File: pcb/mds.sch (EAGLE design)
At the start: 60 parts, among them IC1 MAX1555, U2 ISD1900ISD1932, U5 ATMEGA328

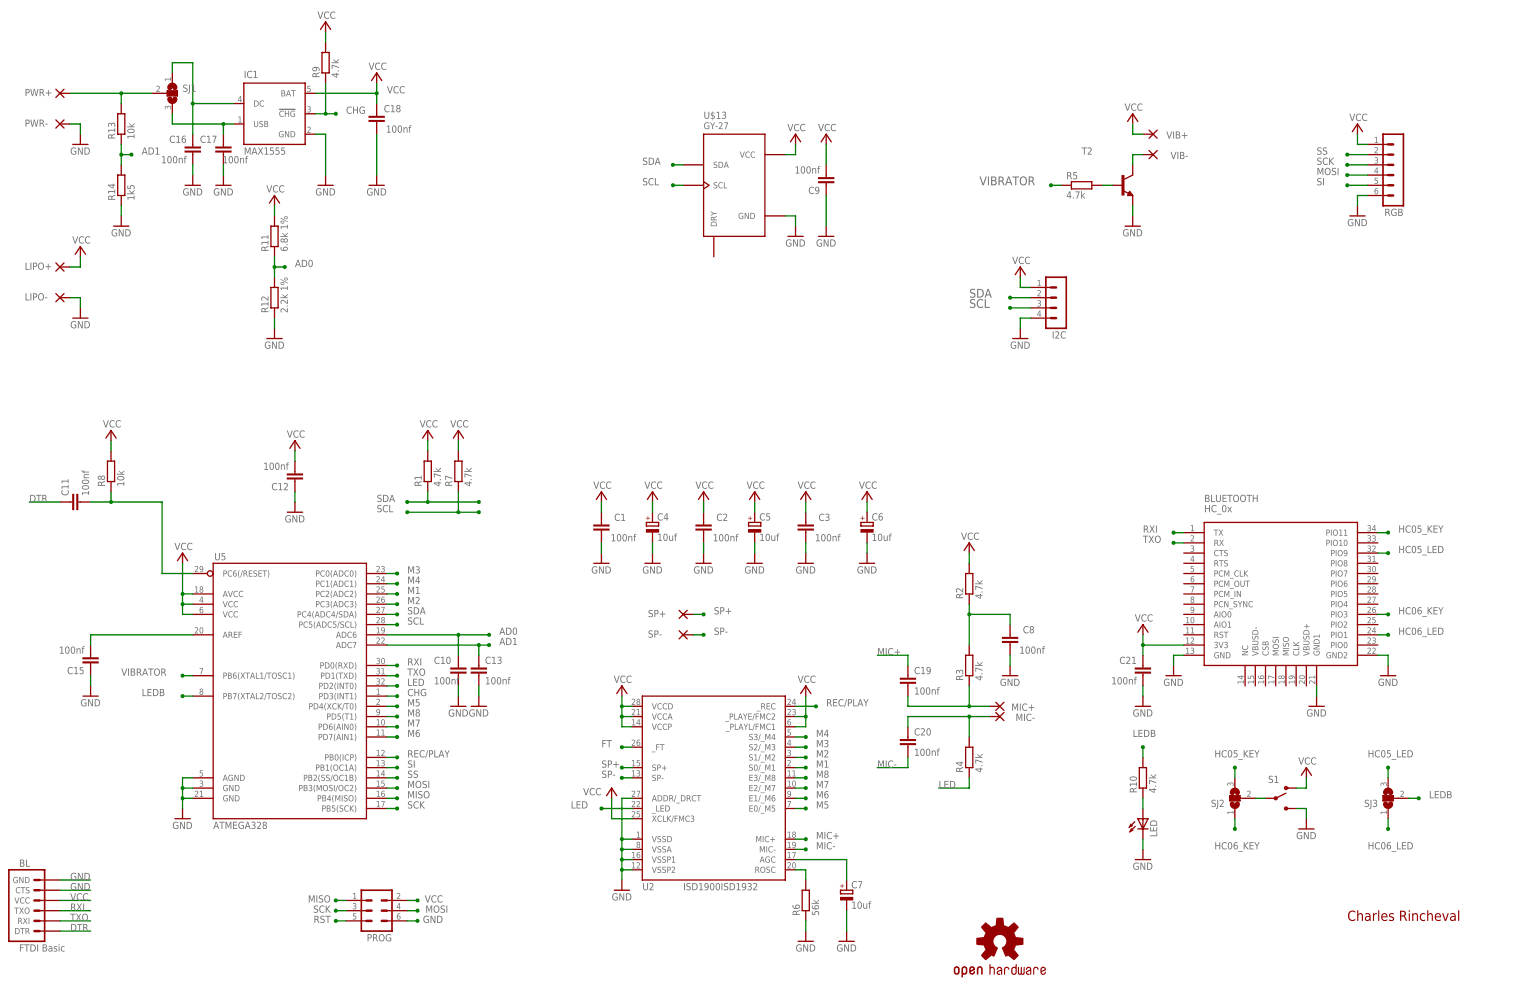
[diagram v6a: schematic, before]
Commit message: Message
- MAX_BRIGHTNESS
- Welcome message
- Charged message
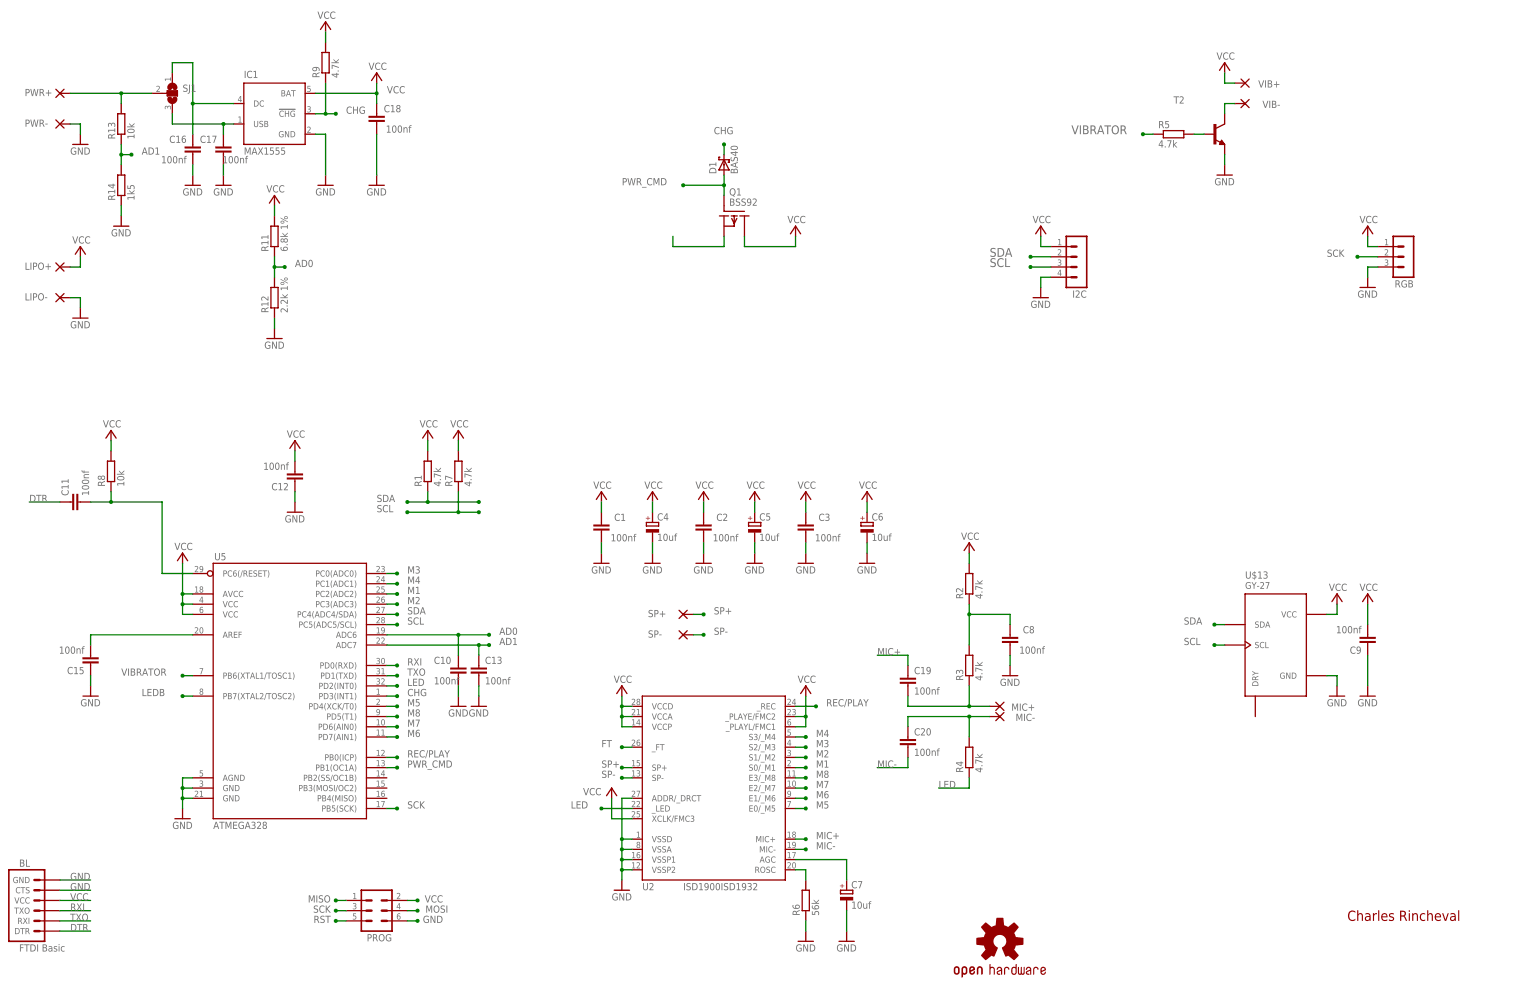
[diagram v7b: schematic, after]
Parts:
- removed BLUETOOTH: HC_0x, Bluetooth HC-05:HC_05
- removed C21: 100nf, rcl:C-EUC0805
- removed LED: (no value), led:LEDCHIP-LED0805
- removed R10: 4.7k, rcl:R-EU_M0805
- removed S1: (no value), SparkFun-Electromechanical:SWITCH-SPDTSMD2
- removed SJ2, SJ3: (no value), jumper:SJ2W
- added D1: BAS40, diode:BAS40
- added Q1: BSS92, transistor-fet:BSS92
- RGB: device con-lstb:MA06-1 -> con-lstb:MA03-1
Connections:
- removed net HC05_KEY: BLUETOOTH.PIO11, SJ2.3
- removed net HC05_LED: BLUETOOTH.PIO9, SJ3.3
- removed net HC06_KEY: BLUETOOTH.PIO3, SJ2.1
- removed net HC06_LED: BLUETOOTH.PIO1, SJ3.1
- removed net N$10: LED.A, R10.1
- removed net SI: RGB.5, U5.PB1(OC1A)
- removed net SS: RGB.2, U5.PB2(SS/OC1B)
- new net PWR_CMD: D1.A, Q1.G, U5.PB1(OC1A)
- net CHG: now also D1.C
- net GND: now also RGB.3; no longer BLUETOOTH.GND, BLUETOOTH.GND1, BLUETOOTH.GND2, C21.1, LED.C, RGB.6, S1.S
- net LEDB: no longer R10.2, SJ3.2
- net MISO: no longer U5.PB4(MISO)
- net MOSI: no longer RGB.4, U5.PB3(MOSI/OC2)
- net N$4: now also Q1.S; no longer S1.P, SJ2.2
- net RXI: no longer BLUETOOTH.TX
- net SCK: now also RGB.2; no longer RGB.3
- net TXO: no longer BLUETOOTH.RX
- net VCC: now also Q1.D; no longer BLUETOOTH.3V3, C21.2, S1.O
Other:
- note added: "If CHG, then power up !"
- note added: "Power control"
- note removed: "Bluetooth"
- moved on the sheet: C9, I2C, R5, T2, U$13, VIB+, VIB-

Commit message: Power control
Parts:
- removed D1: BAS40, diode:BAS40
- removed Q1: BSS92, transistor-fet:BSS92
- added D3, D4: (no value), OPL Eagle Library:D-D1206
- added LDR+, LDR-: (no value), wirepad:1,6/0,8
- added Q2: MOSFET-P, OPL Eagle Library:MOSFET-P-044021001
- added R10, R15: 4.7k, rcl:R-EU_M0805
- added U$1: HMC5883LSMD, SparkFun-Sensors:HMC5883LSMD
- added U3: ADXL345, SparkFun-Sensors:ADXL345
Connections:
- removed net N$4: Q1.S
- new net +UB: LIPO+.P, Q2.S
- new net AD_INT1: U3.INT1, U5.PB2(SS/OC1B)
- new net AD_INT2: U3.INT2, U5.PB3(MOSI/OC2)
- new net LDR: LDR-.P, R15.2
- new net N$13: U5.PB4(MISO)
- new net N$14: U$1.SETP
- new net N$9: D4.-
- net CHG: now also D3.-; no longer D1.C
- net GND: now also R15.1, U$1.GND@1, U$1.GND@2, U3.GND@2, U3.GND@4, U3.GND@5, U3.NC@11, U3.NC@3
- net PWR_CMD: now also D3.+, D4.+, Q2.G, R10.1; no longer D1.A, Q1.G
- net SCL: now also U3.SCL
- net SDA: now also U3.SDA
- net VCC: now also LDR+.P, Q2.D, R10.2, U$1.S1, U$1.VDD, U$1.VDDIO, U3.VDD, U3.VSS; no longer LIPO+.P, Q1.D
